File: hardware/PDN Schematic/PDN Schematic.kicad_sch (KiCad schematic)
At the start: 11 parts, among them J1 Conn_01x02_Pin, J10 Conn_01x02_Pin, J11 Led Indicator Pin, J2 Conn_01x02_Pin, J3 Conn_01x02_Pin, J4 Conn_01x04_Pin, J7 Conn_01x02_Pin, J8 Conn_01x02_Pin, J9 Conn_01x02_Pin, U1 Current Reader

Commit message: almost finalized GSE PDN files
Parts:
- added C1: 220n, Capacitor_SMD:C_0805_2012Metric, symbol Device:C
- U1: footprint GSE_PDN_LIB:INA238_MODULE -> RocketDesignCustomFootprints:INA238_MODULE
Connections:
- net +13V: now also C1.2
- net VOUT: now also C1.1
- net at U1.10 (GND): now also J4.2 (Pin_2)
- net at U1.11 (Vin): now also J4.1 (Pin_1)
- net at U1.4 (ALRT): no longer J4.4 (Pin_4)
- net at U1.5 (Vin+): no longer J4.3 (Pin_3)
- net at U1.6 (Vin-): no longer J4.2 (Pin_2)
- net at U1.7 (VBUS): no longer J4.1 (Pin_1)
- net at U1.8 (SDA): now also J4.4 (Pin_4)
- net at U1.9 (SCL): now also J4.3 (Pin_3)
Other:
- moved on the sheet: J10, J2, J3, J7, J8, J9

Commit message: Extra GSE PDN Board changes
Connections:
- net GND2: now reaches J4.2 (Pin_2), U1.10 (GND)
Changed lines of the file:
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@@
+	)
+	(junction
+		(at 77.47 45.72)
+		(diameter 0)
+		(color 0 0 0 0)
 	)
 	(junction
@@
 	(wire
 		(pts
+			(xy 77.47 45.72) (xy 83.82 45.72)
+		)
+		(stroke
+			(width 0)
+			(type default)
+		)
+	)
+	(wire
+		(pts
+			(xy 68.58 43.18) (xy 83.82 43.18)
+		)
+		(stroke
+			(width 0)
+			(type default)
+		)
+	)
+	(wire
+		(pts
+			(xy 81.28 48.26) (xy 81.28 53.34)
+		)
+		(stroke
+			(width 0)
+			(type default)
+		)
+	)
+	(wire
+		(pts
 			(xy 132.08 85.09) (xy 132.08 55.88)
 		)
@@
 	(wire
 		(pts
+			(xy 68.58 50.8) (xy 71.12 50.8)
+		)
+		(stroke
+			(width 0)
+			(type default)
+		)
+	)
+	(wire
+		(pts
+			(xy 72.39 53.34) (xy 72.39 48.26)
+		)
+		(stroke
+			(width 0)
+			(type default)
+		)
+	)
+	(wire
+		(pts
 			(xy 132.08 55.88) (xy 137.16 55.88)
 		)
@@
 	(wire
 		(pts
+			(xy 81.28 53.34) (xy 72.39 53.34)
+		)
+		(stroke
+			(width 0)
+			(type default)
+		)
+	)
+	(wire
+		(pts
 			(xy 96.52 82.55) (xy 96.52 85.09)
 		)
@@
 	(wire
 		(pts
+			(xy 68.58 45.72) (xy 77.47 45.72)
+		)
+		(stroke
+			(width 0)
+			(type default)
+		)
+	)
+	(wire
+		(pts
+			(xy 82.55 50.8) (xy 82.55 54.61)
+		)
+		(stroke
+			(width 0)
+			(type default)
+		)
+	)
+	(wire
+		(pts
 			(xy 127 91.44) (xy 127 55.88)
 		)
@@
 	(wire
 		(pts
+			(xy 72.39 48.26) (xy 68.58 48.26)
+		)
+		(stroke
+			(width 0)
+			(type default)
+		)
+	)
+	(wire
+		(pts
 			(xy 101.6 54.61) (xy 104.14 54.61)
 		)
@@
 	(wire
 		(pts
+			(xy 83.82 50.8) (xy 82.55 50.8)
+		)
+		(stroke
+			(width 0)
+			(type default)
+		)
+	)
+	(wire
+		(pts
+			(xy 83.82 48.26) (xy 81.28 48.26)
+		)
+		(stroke
+			(width 0)
+			(type default)
+		)
+	)
+	(wire
+		(pts
 			(xy 107.95 55.88) (xy 114.3 55.88)
 		)
@@
 	(wire
 		(pts
+			(xy 71.12 54.61) (xy 82.55 54.61)
+		)
+		(stroke
+			(width 0)
+			(type default)
+		)
+	)
+	(wire
+		(pts
 			(xy 154.94 78.74) (xy 137.16 78.74)
 		)
@@
 		(pts
 			(xy 120.65 55.88) (xy 127 55.88)
+		)
+		(stroke
+			(width 0)
+			(type default)
+		)
+	)
+	(wire
+		(pts
+			(xy 71.12 50.8) (xy 71.12 54.61)
 		)
 		(stroke
@@
 	)
 	(symbol
+		(lib_id "power:GND2")
+		(at 77.47 45.72 0)
+		(unit 1)
+		(exclude_from_sim no)
+		(in_bom yes)
+		(on_board yes)
+		(dnp no)
+		(fields_autoplaced yes)
+		(property "Reference" "#PWR011"
+			(at 77.47 52.07 0)
+			(effects
+				(font
+					(size 1.27 1.27)
+				)
+				(hide yes)
+			)
+		)
+		(property "Value" "GND2"
+			(at 77.47 50.8 0)
+			(effects
+				(font
+					(size 1.27 1.27)
+				)
+			)
+		)
+		(property "Footprint" ""
+			(at 77.47 45.72 0)
+			(effects
+				(font
+					(size 1.27 1.27)
+				)
+				(hide yes)
+			)
+		)
+		(property "Datasheet" ""
+			(at 77.47 45.72 0)
+			(effects
+				(font
+					(size 1.27 1.27)
+				)
+				(hide yes)
+			)
+		)
+		(property "Description" "Power symbol creates a global label with name \"GND2\" , ground"
+			(at 77.47 45.72 0)
+			(effects
+				(font
+					(size 1.27 1.27)
+				)
+				(hide yes)
+			)
+		)
+		(pin "1"
+		)
+		(instances
+			(project ""
+				(path "/659706a1-35a7-4427-a143-52ebb1d5f327"
+					(reference "#PWR011")
+					(unit 1)
+				)
+			)
+		)
+	)
+	(symbol
 		(lib_id "Connector:Conn_01x02_Pin")
 		(at 160.02 106.68 180)
@@
 	(symbol
 		(lib_id "Connector:Conn_01x04_Pin")
-		(at 78.74 45.72 0)
+		(at 63.5 45.72 0)
 		(unit 1)
 		(exclude_from_sim no)
@@
 		(fields_autoplaced yes)
 		(property "Reference" "J4"
-			(at 76.2 46.99 90)
+			(at 60.96 46.99 90)
 			(effects
 				(font
@@
 		)
 		(property "Value" "Conn_01x04_Pin"
-			(at 79.375 40.64 0)
+			(at 64.135 40.64 0)
 			(effects
 				(font
@@
 		)
 		(property "Footprint" "Connector_PinHeader_2.54mm:PinHeader_1x04_P2.54mm_Vertical"
-			(at 78.74 45.72 0)
+			(at 63.5 45.72 0)
 			(effects
 				(font
@@
 		)
 		(property "Datasheet" "~"
-			(at 78.74 45.72 0)
+			(at 63.5 45.72 0)
 			(effects
 				(font
@@
 		)
 		(property "Description" "Generic connector, single row, 01x04, script generated"
-			(at 78.74 45.72 0)
-			(effects
-				(font
+			(at 63.5 45.72 0)
+			(effects
+				(font

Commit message: proper library pathing
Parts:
- U1: footprint RocketDesignCustomFootprints:INA238_MODULE -> GSE_PDN_LIB:INA238_MODULE
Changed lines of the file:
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@@
 			)
 		)
-		(property "Footprint" "RocketDesignCustomFootprints:INA238_MODULE"
+		(property "Footprint" "GSE_PDN_LIB:INA238_MODULE"
 			(at 91.44 52.07 0)
 			(effects

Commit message: Generated build files and added component data
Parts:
- R1: DigiKey (none) -> https://www.digikey.com/en/products/detail/vishay-dale/RCS1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
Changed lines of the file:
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@@
 			)
 		)
-		(property "Datasheet" "~"
+		(property "Datasheet" "https://www.vishay.com/docs/20065/rcse3.pdf"
 			(at 96.52 80.01 0)
 			(effects
@@
 			(at 96.52 80.01 0)
 			(effects
+				(font
+					(size 1.27 1.27)
+				)
+				(hide yes)
+			)
+		)
+		(property "DigiKey" "https://www.digikey.com/en/products/detail/vishay-dale/RCS12061K00FKEA/10059648"
+			(at 96.52 80.01 0)
+			(effects

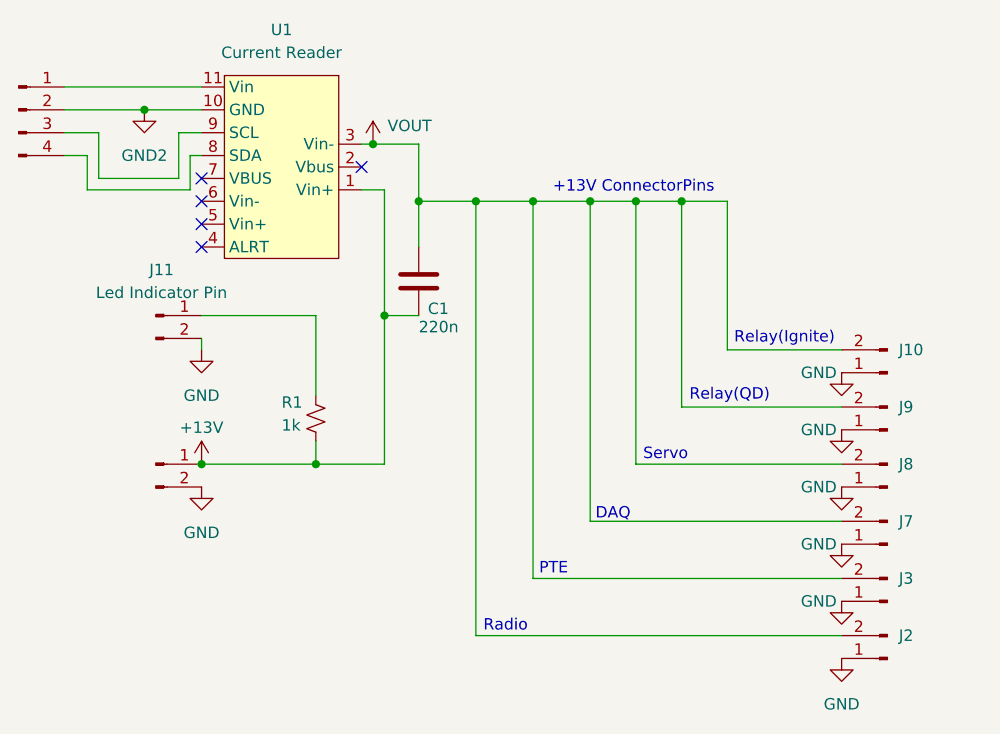
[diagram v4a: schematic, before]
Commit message: Intermediate commit. DAQ code works occasionally (best after 15 mins of power off period!?!?). I think something isn't being configured correctly with the ADC
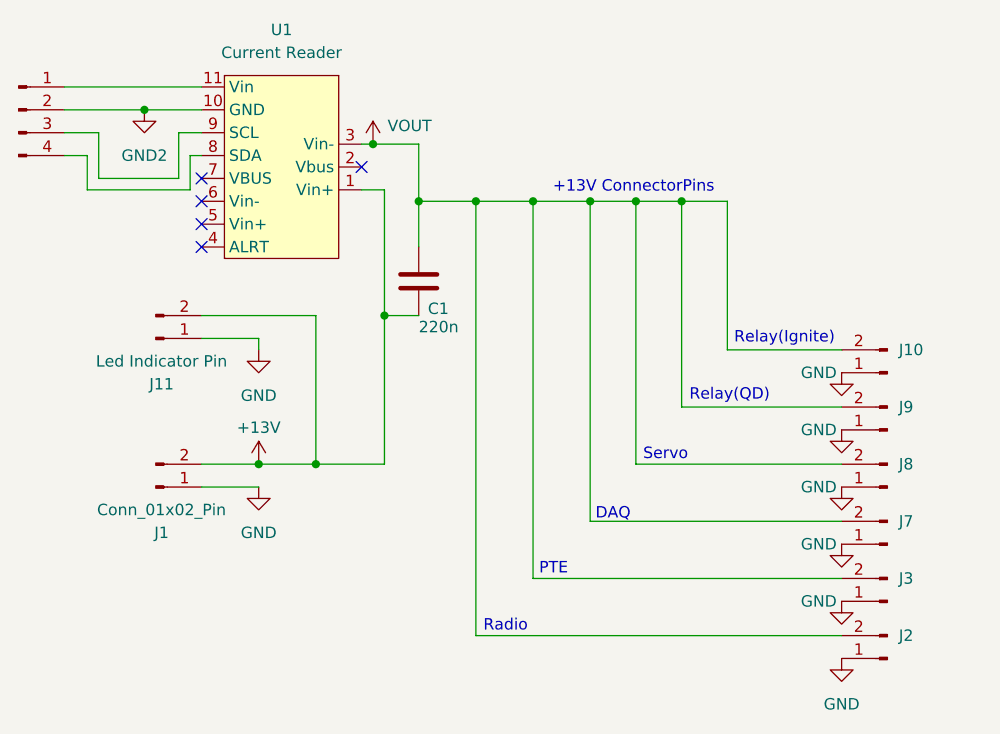
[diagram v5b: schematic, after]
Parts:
- removed R1: 1k, Resistor_SMD:R_1206_3216Metric, symbol Device:R_Small_US
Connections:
- net +13V: now also J1.2 (Pin_2), J11.2 (Pin_2); no longer J1.1 (Pin_1)
- net GND: now also J1.1 (Pin_1), J11.1 (Pin_1); no longer J1.2 (Pin_2), J11.2 (Pin_2)
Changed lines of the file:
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@@
-	)
-	(junction
-		(at 83.82 85.09)
-		(diameter 0)
-		(color 0 0 0 0)
 	)
 	(junction
@@
 	)
 	(junction
+		(at 90.17 85.09)
+		(diameter 0)
+		(color 0 0 0 0)
+	)
+	(junction
 		(at 127 55.88)
 		(diameter 0)
@@
 	(wire
 		(pts
+			(xy 90.17 71.12) (xy 83.82 71.12)
+		)
+		(stroke
+			(width 0)
+			(type default)
+		)
+	)
+	(wire
+		(pts
 			(xy 81.28 53.34) (xy 72.39 53.34)
 		)
@@
 	(wire
 		(pts
-			(xy 96.52 82.55) (xy 96.52 85.09)
+			(xy 96.52 68.58) (xy 96.52 85.09)
 		)
 		(stroke
@@
 	(wire
 		(pts
+			(xy 90.17 85.09) (xy 96.52 85.09)
+		)
+		(stroke
+			(width 0)
+			(type default)
+		)
+	)
+	(wire
+		(pts
 			(xy 101.6 54.61) (xy 104.14 54.61)
 		)
@@
 	(wire
 		(pts
-			(xy 83.82 85.09) (xy 96.52 85.09)
-		)
-		(stroke
-			(width 0)
-			(type default)
-		)
-	)
-	(wire
-		(pts
-			(xy 96.52 77.47) (xy 96.52 68.58)
+			(xy 83.82 85.09) (xy 90.17 85.09)
 		)
 		(stroke
@@
 	(wire
 		(pts
-			(xy 83.82 71.12) (xy 83.82 72.39)
+			(xy 90.17 87.63) (xy 83.82 87.63)
+		)
+		(stroke
+			(width 0)
+			(type default)
+		)
+	)
+	(wire
+		(pts
+			(xy 90.17 71.12) (xy 90.17 72.39)
 		)
 		(stroke
@@
 	(symbol
 		(lib_id "Connector:Conn_01x02_Pin")
-		(at 78.74 68.58 0)
-		(unit 1)
-		(exclude_from_sim no)
-		(in_bom yes)
-		(on_board yes)
-		(dnp no)
-		(fields_autoplaced yes)
+		(at 78.74 71.12 0)
+		(mirror x)
+		(unit 1)
+		(exclude_from_sim no)
+		(in_bom yes)
+		(on_board yes)
+		(dnp no)
 		(property "Reference" "J11"
-			(at 79.375 63.5 0)
+			(at 79.375 76.2 0)
 			(effects
 				(font
@@
 		)
 		(property "Value" "Led Indicator Pin"
-			(at 79.375 66.04 0)
+			(at 79.375 73.66 0)
 			(effects
 				(font
@@
 		)
 		(property "Footprint" "Connector_AMASS:AMASS_XT30U-M_1x02_P5.0mm_Vertical"
-			(at 78.74 68.58 0)
+			(at 78.74 71.12 0)
 			(effects
 				(font
@@
 		)
 		(property "Datasheet" "~"
-			(at 78.74 68.58 0)
+			(at 78.74 71.12 0)
 			(effects
 				(font
@@
 		)
 		(property "Description" "Generic connector, single row, 01x02, script generated"
-			(at 78.74 68.58 0)
+			(at 78.74 71.12 0)
 			(effects
 				(font
@@
 		)
 		(instances
-			(project ""
+			(project "PDN Schematic"
 				(path "/659706a1-35a7-4427-a143-52ebb1d5f327"
 					(reference "J11")
@@
 	(symbol
 		(lib_id "Connector:Conn_01x02_Pin")
-		(at 78.74 85.09 0)
-		(unit 1)
-		(exclude_from_sim no)
-		(in_bom yes)
-		(on_board yes)
-		(dnp no)
-		(fields_autoplaced yes)
+		(at 78.74 87.63 0)
+		(mirror x)
+		(unit 1)
+		(exclude_from_sim no)
+		(in_bom yes)
+		(on_board yes)
+		(dnp no)
 		(property "Reference" "J1"
-			(at 79.375 80.01 0)
-			(effects
-				(font
-					(size 1.27 1.27)
-				)
-				(hide yes)
+			(at 79.375 92.71 0)
+			(effects
+				(font
+					(size 1.27 1.27)
+				)
 			)
 		)
 		(property "Value" "Conn_01x02_Pin"
-			(at 79.375 82.55 0)
-			(effects
-				(font
-					(size 1.27 1.27)
-				)
-				(hide yes)
+			(at 79.375 90.17 0)
+			(effects
+				(font
+					(size 1.27 1.27)
+				)
 			)
 		)
 		(property "Footprint" "Connector_AMASS:AMASS_XT60-M_1x02_P7.20mm_Vertical"
-			(at 78.74 85.09 0)
+			(at 78.74 87.63 0)
 			(effects
 				(font
@@
 		)
 		(property "Datasheet" "~"
-			(at 78.74 85.09 0)
+			(at 78.74 87.63 0)
 			(effects
 				(font
@@
 		)
 		(property "Description" "Generic connector, single row, 01x02, script generated"
-			(at 78.74 85.09 0)
+			(at 78.74 87.63 0)
 			(effects
 				(font
@@
 	(symbol
 		(lib_id "power:GND")
-		(at 83.82 87.63 0)
+		(at 90.17 87.63 0)
 		(unit 1)
 		(exclude_from_sim no)
@@
 		(fields_autoplaced yes)
 		(property "Reference" "#PWR02"
-			(at 83.82 93.98 0)
+			(at 90.17 93.98 0)
 			(effects
 				(font
@@
 		)
 		(property "Value" "GND"
-			(at 83.82 92.71 0)
+			(at 90.17 92.71 0)
 			(effects
 				(font
@@
 		)
 		(property "Footprint" ""
-			(at 83.82 87.63 0)
+			(at 90.17 87.63 0)
 			(effects
 				(font
@@
 		)
 		(property "Datasheet" ""
-			(at 83.82 87.63 0)
+			(at 90.17 87.63 0)
 			(effects
 				(font
@@
 		)
 		(property "Description" "Power symbol creates a global label with name \"GND\" , ground"
-			(at 83.82 87.63 0)
+			(at 90.17 87.63 0)
 			(effects
 				(font
@@
 	)
 	(symbol
-		(lib_id "Device:R_Small_US")
-		(at 96.52 80.01 0)
-		(unit 1)
-		(exclude_from_sim no)
-		(in_bom yes)
-		(on_board yes)
-		(dnp no)
-		(property "Reference" "R1"
-			(at 92.71 78.232 0)
-			(effects
-				(font
-					(size 1.27 1.27)
-				)
-				(justify left)
-			)
-		)
-		(property "Value" "1k"
-			(at 92.71 80.772 0)
-			(effects
-				(font
-					(size 1.27 1.27)
-				)
-				(justify left)
-			)
-		)
-		(property "Footprint" "Resistor_SMD:R_1206_3216Metric"
-			(at 96.52 80.01 0)
-			(effects
-				(font
-					(size 1.27 1.27)
-				)
-				(hide yes)
-			)
-		)
-		(property "Datasheet" "https://www.vishay.com/docs/20065/rcse3.pdf"
-			(at 96.52 80.01 0)
-			(effects
-				(font
-					(size 1.27 1.27)
-				)
-				(hide yes)
-			)
-		)
-		(property "Description" "Resistor, small US symbol"
-			(at 96.52 80.01 0)
-			(effects
-				(font
-					(size 1.27 1.27)
-				)
-				(hide yes)
-			)
-		)
-		(property "DigiKey" "https://www.digikey.com/en/products/detail/vishay-dale/RCS12061K00FKEA/10059648"
-			(at 96.52 80.01 0)
-			(effects
-				(font
-					(size 1.27 1.27)
-				)
-				(hide yes)
-			)
-		)
-		(pin "1"
-		)
-		(pin "2"
-		)
-		(instances
-			(project ""
-				(path "/659706a1-35a7-4427-a143-52ebb1d5f327"
-					(reference "R1")
-					(unit 1)
-				)
-			)
-		)
-	)
-	(symbol
 		(lib_id "power:GND")
 		(at 154.94 87.63 0)
@@
 	(symbol
 		(lib_id "power:+12V")
-		(at 83.82 85.09 0)
+		(at 90.17 85.09 0)
 		(unit 1)
 		(exclude_from_sim no)
@@
 		(dnp no)
 		(property "Reference" "#PWR01"
-			(at 83.82 88.9 0)
+			(at 90.17 88.9 0)
 			(effects
 				(font
@@
 		)
 		(property "Value" "+13V"
-			(at 83.82 81.026 0)
+			(at 90.17 81.026 0)
 			(effects
 				(font
@@
 		)
 		(property "Footprint" ""
-			(at 83.82 85.09 0)
+			(at 90.17 85.09 0)
 			(effects
 				(font
@@
 		)
 		(property "Datasheet" ""
-			(at 83.82 85.09 0)
+			(at 90.17 85.09 0)
 			(effects
 				(font
@@
 		)
 		(property "Description" "Power symbol creates a global label with name \"+12V\""
-			(at 83.82 85.09 0)
+			(at 90.17 85.09 0)
 			(effects
 				(font
@@
 	(symbol
 		(lib_id "power:GND")
-		(at 83.82 72.39 0)
+		(at 90.17 72.39 0)
 		(unit 1)
 		(exclude_from_sim no)
@@
 		(fields_autoplaced yes)
 		(property "Reference" "#PWR09"
-			(at 83.82 78.74 0)
+			(at 90.17 78.74 0)
 			(effects
 				(font
@@
 		)
 		(property "Value" "GND"
-			(at 83.82 77.47 0)
+			(at 90.17 77.47 0)
 			(effects
 				(font
@@
 		)
 		(property "Footprint" ""
-			(at 83.82 72.39 0)
+			(at 90.17 72.39 0)
 			(effects
 				(font
@@
 		)
 		(property "Datasheet" ""
-			(at 83.82 72.39 0)
+			(at 90.17 72.39 0)
 			(effects
 				(font
@@
 		)
 		(property "Description" "Power symbol creates a global label with name \"GND\" , ground"
-			(at 83.82 72.39 0)
-			(effects
-				(font
+			(at 90.17 72.39 0)
+			(effects
+				(font
